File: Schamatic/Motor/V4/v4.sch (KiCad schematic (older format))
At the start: 45 parts, among them J1 SWD, J10 GND, J11 V, J12 U, J13 W, J2 SPI, J3 RS485, J4 RS485, J5 12, J6 12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

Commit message: ordered controller
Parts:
- removed C3: 1uF, Capacitors_SMD:C_0805, symbol C_Small
- removed R1: 47K, Resistors_SMD:R_0805, symbol R
- removed R2: 3K, Resistors_SMD:R_0805, symbol R
- added J14: A0, Pin_Headers:Pin_Header_Straight_1x01_Pitch2.54mm, symbol CONN_01X01
- C1: value 47uF -> 100uF
- C2: value 47uF -> 22uF
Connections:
- net +3V3: now also J2.6 (P6); no longer J2.1 (P1)
- net CS: now also J2.4 (P4); no longer J2.6 (P6)
- net Earth: now also J2.5 (P5); no longer J2.2 (P2)
- net MISO: now also J2.2 (P2); no longer J2.4 (P4)
- net MOSI: now also J2.1 (P1); no longer J2.3 (P3)
- net SCK: now also J2.3 (P3); no longer J2.5 (P5)
- net at U1.11 (PA0): now also J14.1 (P1)

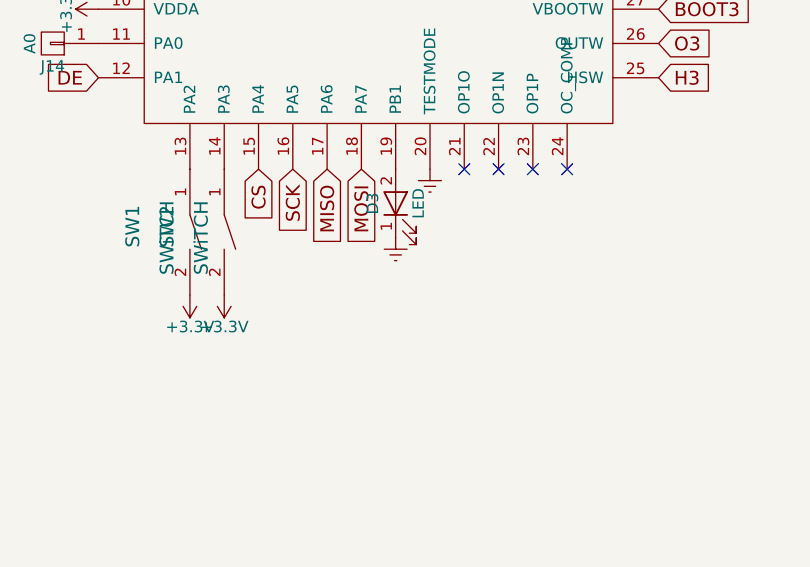
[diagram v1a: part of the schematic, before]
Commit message: button press and external clock
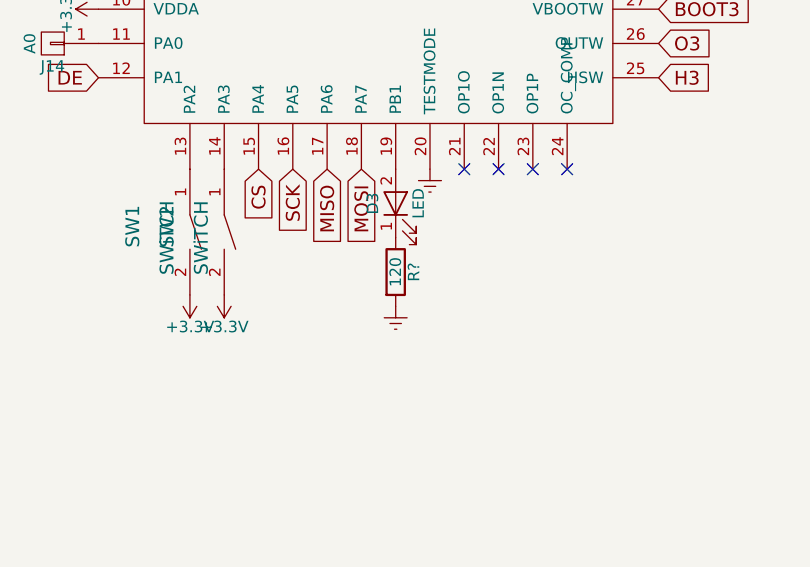
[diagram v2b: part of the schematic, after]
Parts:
- added R?: 120, Resistors_SMD:R_0805, symbol R
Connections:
- net Earth: now also R?.2; no longer D3.1 (K)
- new net: D3.1 (K), R?.1
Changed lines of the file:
@@
 L Earth #PWR26
 U 1 1 59C94575
-P 3950 4500
-F 0 "#PWR26" H 3950 4250 50  0001 C CNN
-F 1 "Earth" H 3950 4350 50  0001 C CNN
-F 2 "" H 3950 4500 50  0001 C CNN
-F 3 "" H 3950 4500 50  0001 C CNN
-	1    3950 4500
+P 3950 4800
+F 0 "#PWR26" H 3950 4550 50  0001 C CNN
+F 1 "Earth" H 3950 4650 50  0001 C CNN
+F 2 "" H 3950 4800 50  0001 C CNN
+F 3 "" H 3950 4800 50  0001 C CNN
+	1    3950 4800
 	1    0    0    -1
 $EndComp
@@
 	-1   0    0    1
 $EndComp
+$Comp
+L R R?
+U 1 1 59E5FB9B
+P 3950 4650
+F 0 "R?" V 4030 4650 50  0000 C CNN
+F 1 "120" V 3950 4650 50  0000 C CNN
+F 2 "Resistors_SMD:R_0805" V 3880 4650 50  0001 C CNN
+F 3 "" H 3950 4650 50  0001 C CNN
+	1    3950 4650
+	1    0    0    -1
+$EndComp
 $EndSCHEMATC

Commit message: spi comm
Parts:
- gave numbers to parts that had none: 1
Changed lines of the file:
@@
 $EndComp
 $Comp
-L R R?
+L R R1
 U 1 1 59E5FB9B
 P 3950 4650
-F 0 "R?" V 4030 4650 50  0000 C CNN
+F 0 "R1" V 4030 4650 50  0000 C CNN
 F 1 "120" V 3950 4650 50  0000 C CNN
 F 2 "Resistors_SMD:R_0805" V 3880 4650 50  0001 C CNN

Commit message: DE pin for USART
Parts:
- U2: value RS-485 -> MAX14840EASA+
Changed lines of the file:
@@
 P 3000 6750
 F 0 "U2" H 3150 7000 60  0000 C CNN
-F 1 "RS-485" H 3150 7350 60  0000 C CNN
+F 1 "MAX14840EASA+" H 3150 7350 60  0000 C CNN
 F 2 "Housings_SOIC:SOIC-8_3.9x4.9mm_Pitch1.27mm" H 3000 6750 60  0001 C CNN
 F 3 "" H 3000 6750 60  0001 C CNN
